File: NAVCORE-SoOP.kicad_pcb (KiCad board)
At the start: 6 copper layers, 45 x 46 mm, 148 parts, among them J1 USB-C, J2 ESC 8P, J3 GPS+I2C, J8 microSD, P41 TEL_5V, P42 TEL_TX, P43 TEL_RX, P44 TEL_PPS, P45 TEL_RTS, P46 TEL_GND, P51 RC_5V, P52 RC_TX, P53 RC_RX, P54 RC_GND, P61 CAN_5V, P62 CANH, P63 CANL, P64 CAN_GND, P71 RF_5V, P72 RF_TX, P73 RF_RX, P74 RF_GND, Q1 AO3400A, Q3 AO3400A, SW1 BOOT, SW2 RESET, U1 STM32H743VIT6, U10 TLV75533, U11 SN65HVD230, U12 USBLC6-2SC6, U17 74LVC1G17, U18 TPS54202, U2 ICM-42688-P, U3 ICM-42605, U4 MS5611, U5 W25Q128JVSIQ, U6 PMW3901, U7 VL53L1X, U8 TPS54202, U9 AP2112K-3.3, Y1 8MHz

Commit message: rev B re-layout and re-route
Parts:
- removed C37, C38, C39: 100n, Capacitor_SMD:C_0402_1005Metric
- removed C40: 4u7, Capacitor_SMD:C_0805_2012Metric
- removed P42: TEL_TX, TestPoint:TestPoint_Pad_1.5x1.5mm
- removed P43: TEL_RX, TestPoint:TestPoint_Pad_1.5x1.5mm
- removed P45: TEL_RTS, TestPoint:TestPoint_Pad_1.5x1.5mm
- removed P51: RC_5V, TestPoint:TestPoint_Pad_1.5x1.5mm
- removed P52: RC_TX, TestPoint:TestPoint_Pad_1.5x1.5mm
- removed P53: RC_RX, TestPoint:TestPoint_Pad_1.5x1.5mm
- removed P54: RC_GND, TestPoint:TestPoint_Pad_1.5x1.5mm
- removed R13: 10k, Resistor_SMD:R_0402_1005Metric
- removed U6: PMW3901, jlc:COB-28_L6.0-W6.0-P0.65-TL-EP
- removed U7: VL53L1X, jlc:OPTO-SMD_VL53L1CXV0FY-1
- added C49: 100n, Capacitor_SMD:C_0402_1005Metric, B.Cu at (135.6, 112.6)
- added C50: 100n, Capacitor_SMD:C_0402_1005Metric, B.Cu at (143.3, 116.0)
- added C51: 1u, Capacitor_SMD:C_0402_1005Metric, B.Cu at (140.5, 120.8)
- added C52: 100p, Capacitor_SMD:C_0402_1005Metric, B.Cu at (138.1, 104.0)
- added C56: 10n, Capacitor_SMD:C_0402_1005Metric, B.Cu at (143.3, 117.2)
- added C57: 10n, Capacitor_SMD:C_0402_1005Metric, B.Cu at (143.3, 119.5)
- added C58: 1n, Capacitor_SMD:C_0402_1005Metric, B.Cu at (142.5, 120.7)
- added C59: 100n, Capacitor_SMD:C_0402_1005Metric, B.Cu at (134.0, 121.4)
- added C60: 100n, Capacitor_SMD:C_0402_1005Metric, B.Cu at (143.3, 114.3)
- added C61: 100n, Capacitor_SMD:C_0402_1005Metric, B.Cu at (134.6, 118.0)
- added C62: 100n, Capacitor_SMD:C_0402_1005Metric, B.Cu at (134.1, 119.1)
- added C63: 100n, Capacitor_SMD:C_0402_1005Metric, B.Cu at (134.1, 120.2)
- added C64: 100n, Capacitor_SMD:C_0402_1005Metric, B.Cu at (133.7, 115.3)
- added DZ1: BZT52C15, jlc:SOD-123_L2.7-W1.6-LS3.7-RD, B.Cu at (107.2, 103.3)
- added J11: SERIAL2 4P, jlc:CONN-SMD_4P-P1.00_SM04B-SRSS-TB-LF-SN, B.Cu at (103.8, 132.8)
- added J12: U.FL ANT, Connector_Coaxial:U.FL_Hirose_U.FL-R-SMT-1_Vertical, F.Cu at (130.9, 103.5)
- added J5: RC IN, jlc:CONN-SMD_4P-P1.00_SM04B-SRSS-TB-LF-SN, B.Cu at (141.7, 130.9)
- added J9: I2C 4P, jlc:CONN-SMD_4P-P1.00_SM04B-SRSS-TB-LF-SN, F.Cu at (103.6, 129.8)
- added Q4: WST4041, jlc:SOT-23-3_L2.9-W1.3-P1.90-LS2.4-BR, B.Cu at (102.5, 104.0)
- added R28: 0R, Resistor_SMD:R_0402_1005Metric, B.Cu at (137.6, 111.6)
- added R29: 0R, Resistor_SMD:R_0402_1005Metric, B.Cu at (134.3, 113.7)
- added R30: 10k, Resistor_SMD:R_0402_1005Metric, B.Cu at (136.6, 121.2)
- added R31: 10k, Resistor_SMD:R_0402_1005Metric, B.Cu at (129.9, 113.0)
- added R34: 1k, Resistor_SMD:R_0402_1005Metric, B.Cu at (143.3, 118.3)
- added R35: 1k, Resistor_SMD:R_0402_1005Metric, B.Cu at (141.0, 112.2)
- added R36: 4k7, Resistor_SMD:R_0402_1005Metric, B.Cu at (104.0, 101.5)
- added R37: 4k7, Resistor_SMD:R_0402_1005Metric, B.Cu at (135.1, 116.4)
- added R46: 100k, Resistor_SMD:R_0402_1005Metric, B.Cu at (106.0, 101.2)
- added TP22: VSERVO, TestPoint:TestPoint_Pad_1.5x1.5mm, F.Cu at (105.0, 101.8)
- added U13: MAX2112, TQFN-28_L5.0-W5.0-P0.50-BL-EP3.3, B.Cu at (139.1, 117.0)
- added U14: OPA2374, jlc:SOP-8_L4.9-W3.9-P1.27-LS6.0-BL, B.Cu at (103.8, 114.0)
- added Y2: 25MHz TCXO, jlc:OSC-SMD_4P-L3.2-W2.5-BL, B.Cu at (141.8, 123.5)
- C1, C10, C11, C12, C13, C14, C15, C16, C19, C2, C21, C26, C27, C28, C29, C3, C30, C31, C32, C33, C34, C35, C36, C4, C41, C43, C44, C46, C5, C65, C66, C68, C73, C8, C9: footprint Capacitor_SMD:C_0402_1005Metric -> C_0402_1005Metric
- C17, C18, C22, C23, C69, C70: footprint Capacitor_SMD:C_1206_3216Metric -> C_1206_3216Metric
- C42, C45, C6, C7: footprint Capacitor_SMD:C_0805_2012Metric -> C_0805_2012Metric
- D1: footprint jlc:DO-214AA_L4.4-W3.6-LS5.3-RD -> DO-214AA_L4.4-W3.6-LS5.3-RD
- D4: footprint jlc:SOD-123F_L2.7-W1.6-LS3.8-RD -> SOD-123F_L2.7-W1.6-LS3.8-RD
- L1: footprint Inductor_SMD:L_0805_2012Metric -> L_0805_2012Metric
- L5: footprint Inductor_SMD:L_1210_3225Metric -> L_1210_3225Metric
- PV1, TP5, TP6: moved to B.Cu
- R10, R11, R12, R18, R19, R38, R39, R4, R40, R41, R42, R43, R5, R6, R7, R9: footprint Resistor_SMD:R_0402_1005Metric -> R_0402_1005Metric
- SW1, SW2: footprint Button_Switch_SMD:SW_SPST_B3U-1000P -> SW_SPST_B3U-1000P
- U12: footprint jlc:SOT-23-6_L2.9-W1.6-P0.95-LS2.8-BL -> SOT-23-6_L2.9-W1.6-P0.95-LS2.8-BL
- U18, U8: footprint SOT-23-6_L2.9-W1.6-P0.95-LS2.8-BL -> jlc:SOT-23-6_L2.9-W1.6-P0.95-LS2.8-BL
- moved PV1 44.8 mm to (111.5, 139.9)
- moved TP4 41.6 mm to (141.9, 126.0)
- moved TP1 38.8 mm to (108.3, 111.5)
- moved TP2 38.7 mm to (104.5, 135.4)
- moved TP5 37.7 mm to (111.5, 102.0), turned to 180 degrees
- moved P63 37.7 mm to (131.9, 117.5)
- moved PL2 36.9 mm to (103.5, 139.9), turned to 180 degrees
- moved P62 35.8 mm to (128.9, 117.5)
- moved R15 27.5 mm to (108.5, 125.5)
- moved R14 24.7 mm to (108.5, 124.0)
- moved P41 22.5 mm to (128.4, 125.0), turned to 180 degrees
- moved U17 22.5 mm to (132.8, 142.2)
- moved TP3 20.0 mm to (123.0, 134.4)
- moved TP6 19.6 mm to (114.0, 122.8), turned to 180 degrees
- moved PL3 18.1 mm to (134.1, 124.7), turned to 180 degrees
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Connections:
- D1 pad 2: VBAT -> VBAT_IN
- J2 pad 2: VBAT -> VBAT_IN
- U1 pad 57: TOF_INT -> (no net)
- U1 pad 58: TOF_XSHUT -> (no net)
- U1 pad 85: EXT_CS1 -> (no net)
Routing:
- net +3V3: track 453.4 -> 119.5 mm, vias 46 -> 14
- net +5V: track 245.7 -> 170.2 mm, vias 46 -> 21
- net +3V3A: track 183.2 -> 124.8 mm, vias 14 -> 7
- net QOUT_N: track 0.00 -> 49.6 mm, vias 0 -> 4
- net IOUT_P: track 0.00 -> 45.9 mm, vias 0 -> 3
- net SOOP_I_ADC: track 35.0 -> 76.1 mm, vias 3 -> 2
- net SWDIO: track 48.7 -> 7.73 mm
- net +9V: track 79.1 -> 38.8 mm, vias 5 -> 0
- net TOF_XSHUT: track 40.3 -> 0.00 mm, vias 3 -> 0
- net QOUT_P: track 0.00 -> 40.1 mm, vias 0 -> 2
- net OPA_IN1N: track 0.00 -> 35.1 mm, vias 0 -> 2
- net UART7_TX: track 33.9 -> 0.00 mm, vias 2 -> 0
- net VCC_RF: track 0.00 -> 33.3 mm, vias 0 -> 2
- net UART7_RTS: track 29.4 -> 0.00 mm, vias 2 -> 0
- net CANH: track 74.8 -> 46.8 mm, vias 3 -> 4
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- removed copper zone on In4.Cu, net +9V

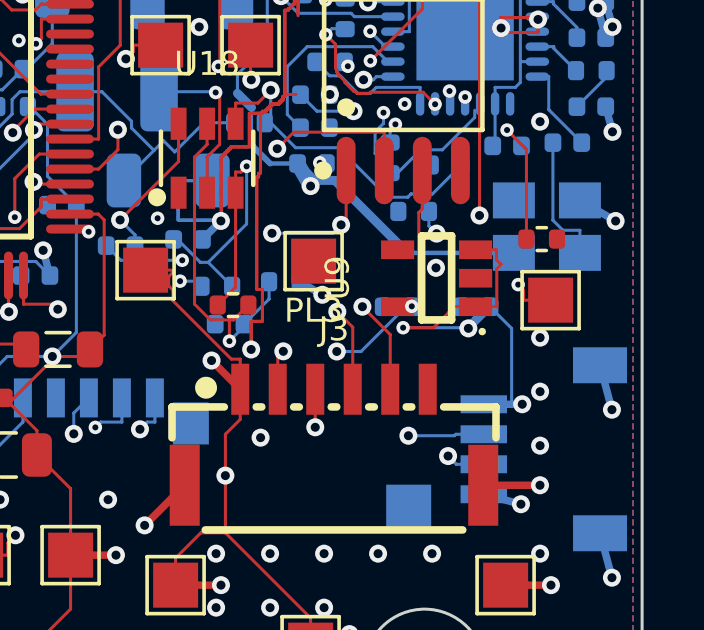
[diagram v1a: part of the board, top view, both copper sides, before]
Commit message: Five more thermal vias on U9, which is the only lever the design has
U9 is the board's worst thermal item: its peak junction models at 179 C on the AP2112
datasheet's explicitly "No Heatsink" theta_JA of 184 C/W, against a 150 C limit, and at
116 C on the SBVS293 EVM figure of 100.8 C/W. A SOT-23-5 has no thermal pad, so every
joule leaves through the leads into whatever copper is attached to them. That copper is
the only thing the layout can change.

Attached copper, measured from the board rather than asserted:

  U9.2 (GND)   1 -> 2 vias,  7699 mm2 of GND plane
  U9.5 (+3V3)  1 -> 2 vias,   700 mm2
  U9.1 (+5V)   1 -> 4 vias,   454 mm2
  U9.3 (+5V)   0 vias - no legal position within 1.7 mm

Vias are offset from the pad with a stub, never in-pad: an unfilled via inside a pad
wicks solder off the joint during reflow.

THIS DOES NOT CLOSE THE THERMAL QUESTION and nothing at a desk can. More copper cannot
make theta_JA worse, so the bound moves in the safe direction, but turning "4 vias and
454 mm2" into a number in C/W needs a thermocouple. docs/BUILD.md T3a still stands, and
the preflight warning still stands with it. The AP2112 has thermal shutdown, so being
wrong means a mid-flight brownout rather than smoke.

DRC 0 errors. Gerbers, drill, all three BOM/CPL pairs and the bundle regenerated;
preflight RC=0, 71 pass, 4 warnings.
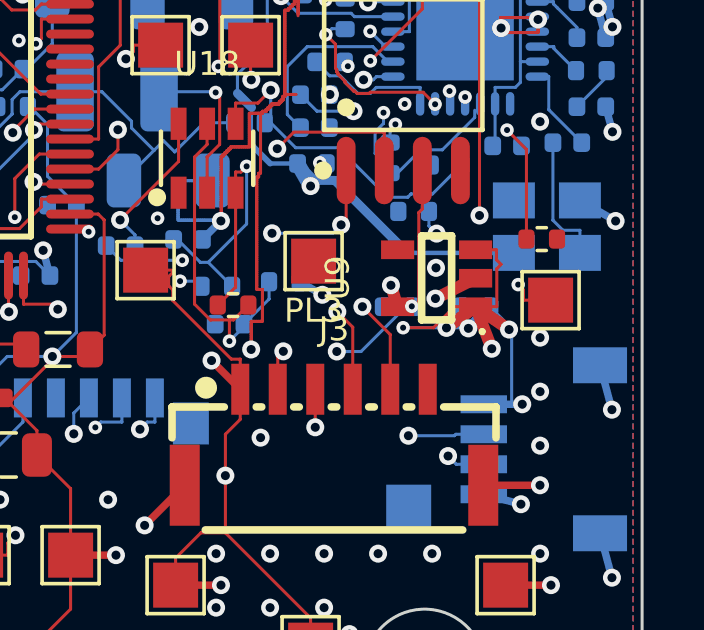
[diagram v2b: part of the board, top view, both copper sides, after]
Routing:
- net +5V: track 170.2 -> 174.2 mm, vias 21 -> 24
- net GND: track 260.8 -> 262.3 mm, vias 153 -> 154
- net +3V3: track 119.5 -> 120.2 mm, vias 14 -> 15
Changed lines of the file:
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@@
 	)
 	(segment
+		(start 139.449975 125.220533)
+		(end 138.111196 125.897048)
+		(width 0.4)
+		(layer "F.Cu")
+		(net 1)
+	)
+	(segment
 		(start 121.21875 125.46875)
 		(end 121.21875 125.53125)
@@
 	)
 	(via
+		(at 138.111196 125.897048)
+		(size 0.6)
+		(drill 0.3)
+		(layers "F.Cu" "B.Cu")
+		(net 1)
+	)
+	(via
 		(at 115.845353 115.894647)
 		(size 0.6)
@@
 	)
 	(segment
+		(start 139.449975 126.169733)
+		(end 140.565397 126.930215)
+		(width 0.4)
+		(layer "F.Cu")
+		(net 4)
+	)
+	(segment
 		(start 133.34375 106.46875)
 		(end 133.28125 106.46875)
@@
 	)
 	(segment
+		(start 139.449975 126.169733)
+		(end 138.479154 126.875075)
+		(width 0.4)
+		(layer "F.Cu")
+		(net 4)
+	)
+	(segment
 		(start 129.3541 124.95)
 		(end 129.3541 125.0259)
@@
 	)
 	(segment
+		(start 139.449975 126.169733)
+		(end 139.989086 127.569503)
+		(width 0.4)
+		(layer "F.Cu")
+		(net 4)
+	)
+	(segment
 		(start 131.308 127.9159)
 		(end 131.605 127.9159)
@@
 	)
 	(via
+		(at 140.565397 126.930215)
+		(size 0.6)
+		(drill 0.3)
+		(layers "F.Cu" "B.Cu")
+		(net 4)
+	)
+	(via
 		(at 132.2446 107.95)
 		(size 0.6)
@@
 		(net 4)
 	)
+	(via
+		(at 139.989086 127.569503)
+		(size 0.6)
+		(drill 0.3)
+		(layers "F.Cu" "B.Cu")
+		(net 4)
+	)
+	(via
+		(at 138.479154 126.875075)
+		(size 0.6)
+		(drill 0.3)
+		(layers "F.Cu" "B.Cu")
+		(net 4)
+	)
 	(segment
 		(start 139.93 126.1697)
@@
 	)
 	(segment
+		(start 136.850025 126.169733)
+		(end 136.627818 125.453406)
+		(width 0.4)
+		(layer "F.Cu")
+		(net 5)
+	)
+	(segment
 		(start 110.84375 123.59375)
 		(end 110.84375 123.65625)
@@
 		(size 0.6)
 		(drill 0.3)
+		(layers "F.Cu" "B.Cu")
+		(net 5)
+	)
+	(via
+		(at 136.627818 125.453406)
+		(size 0.6)
+		(drill 0.3)

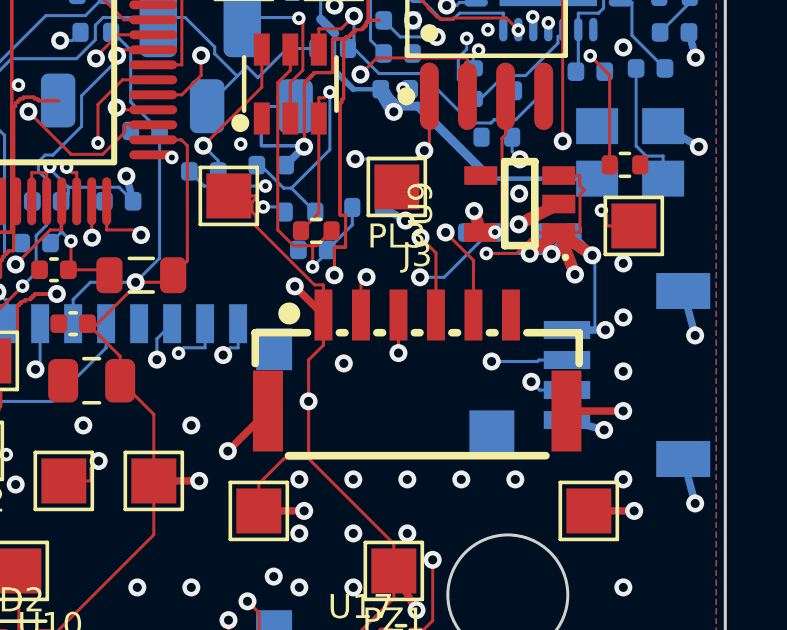
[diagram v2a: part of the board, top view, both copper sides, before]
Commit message: re-route with freerouting and add the U19 temperature sensor
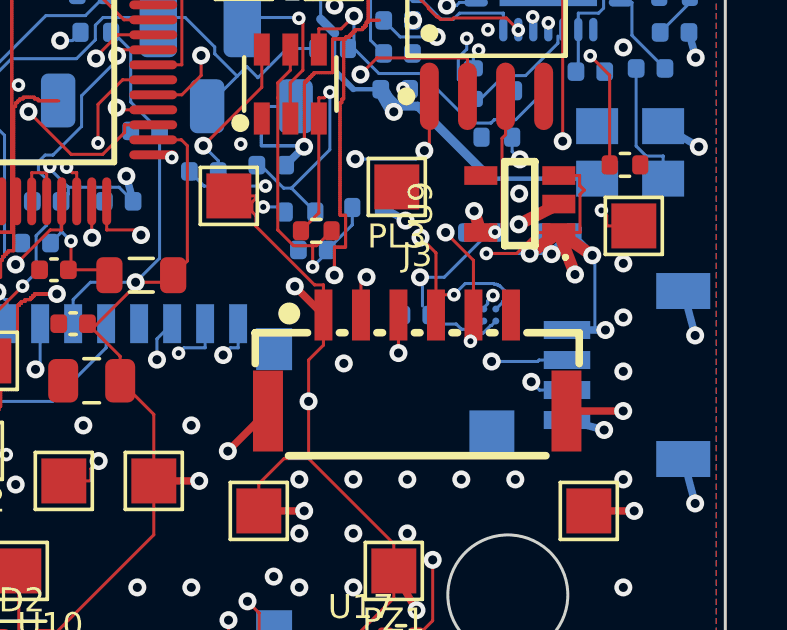
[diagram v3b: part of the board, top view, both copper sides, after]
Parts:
- added C74: 100n, C_0402_1005Metric, B.Cu at (134.7, 128.9)
- added U19: TMP119, DSBGA-6_L1.5-W1.0-R2-C3-P0.40-BL, B.Cu at (136.9, 128.9)
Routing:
- net I2C1_SCL: track 55.3 -> 58.2 mm, vias 3 -> 4
- net +3V3: track 120.2 -> 122.5 mm
- net I2C1_SDA: track 46.4 -> 47.4 mm, vias 3 -> 4
- net GND: track 262.3 -> 262.8 mm, vias 154 -> 155
